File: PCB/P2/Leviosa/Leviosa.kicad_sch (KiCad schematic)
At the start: 52 parts, among them J1 2.54mm 1x03 Servo 1, J2 2.54mm 1x03 Servo 1, J3 2.54mm 1x03 Spare, J4 Barrel_Jack, Q3 TIP122, Q4 TIP122, U1 LM324, U2 ATtiny13A-P, U3 TPS1H200AQDGNRQ1, U4 AMS1117-5.0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

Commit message: update some PCB components as part of P2 iteration
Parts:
- removed D1: BZT52C8V2 WD, Diode_SMD:D_SOD-123, symbol Device:D_Zener
- removed D2, D3: LED, LED_SMD:LED_0805_2012Metric, symbol Device:LED
- removed JP1, JP2, JP3, JP4, JP5, JP6: SolderJumper_2_Open, Jumper:SolderJumper-2_P1.3mm_Open_Pad1.0x1.5mm, symbol Jumper:SolderJumper_2_Open
- removed Pot2: 3362S-1-103LF, Potentiometer_THT:Potentiometer_ACP_CA6-H2,5_Horizontal, symbol Device:R_Potentiometer_US
- removed Q3, Q4: TIP122, Package_TO_SOT_THT:TO-220-3_Vertical, symbol Transistor_BJT:TIP122
- removed R7: 1kΩ, Resistor_SMD:R_0805_2012Metric_Pad1.20x1.40mm_HandSolder, symbol Device:R_US
- removed R8: 400, Resistor_SMD:R_0805_2012Metric_Pad1.20x1.40mm_HandSolder, symbol Device:R_US
- removed U1: LM324, Package_DIP:DIP-14_W7.62mm, symbol Amplifier_Operational:LM324
- added Q1, Q2: NCE0110K, Package_TO_SOT_SMD:TO-252-2, symbol Transistor_FET:DMN61D8LQ
- added U5: LM393, Package_SO:SOIC-8_5.3x5.3mm_P1.27mm, symbol Comparator:LM393
- C4: value 10µF -> 22µF
- R2: value 100kΩ -> 51kΩ; Link https://jlcpcb.com/partdetail/738376-RCT06100KFLF/C702843 -> https://jlcpcb.com/partdetail/23923-0603WAF5102T5E/C23196
- R3: value 7.8kΩ -> 4kΩ
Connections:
- net 5V: now also U5.8 (V+)
- net GND: now also Q2.3 (D), U5.4 (V-)
- net PB2: no longer U6.3 (VOUT)
- net coil_output: now also Q1.2 (S)
- net no_magnet_point: now also U5.5 (+)
- net no_magnet_point_trigger: now also U5.7
- net set_point: now also U5.2 (-)
- net set_point_trigger: now also U5.1
- net transistor1_output: now also Q1.3 (D), Q2.2 (S)
- net at R1.1, TP6.1: now also Q1.1 (G)
- net at R6.1, TP7.1: now also Q2.1 (G)
- new net hall_output: U5.3 (+), U5.6 (-), U6.3 (VOUT)
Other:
- note added: "(12V - 9.6V)/5ma = 460 Ohm minimum"
- note added: "TODO change from voltage divider to a static set point. Check setup to ensure correct voltage set here."
- note added: "TODO: current sense from coil"
- note added: "voltage divider: ~[0.308V, 1.077V] ~[63, 220] analogRead()"
- note removed: "(12V - 9.6V)/5ma = 460 Not sure if this calc is right so keep it to 1K for now"
- note removed: "(5V - 2.2V)/ 5ma = 560"
- note removed: "See (1)"
- note removed: "voltage divider: ~[0.331V, 0.756V] ~[68, 155] analogRead()"
- note removed: "voltage divider: ~[1.65V, 1.96V] ~[337, 399] analogRead()"
- moved on the sheet: C1, C2, C4, D4, D6, R13, R14, R9, TP1, TP2, TP4, U3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

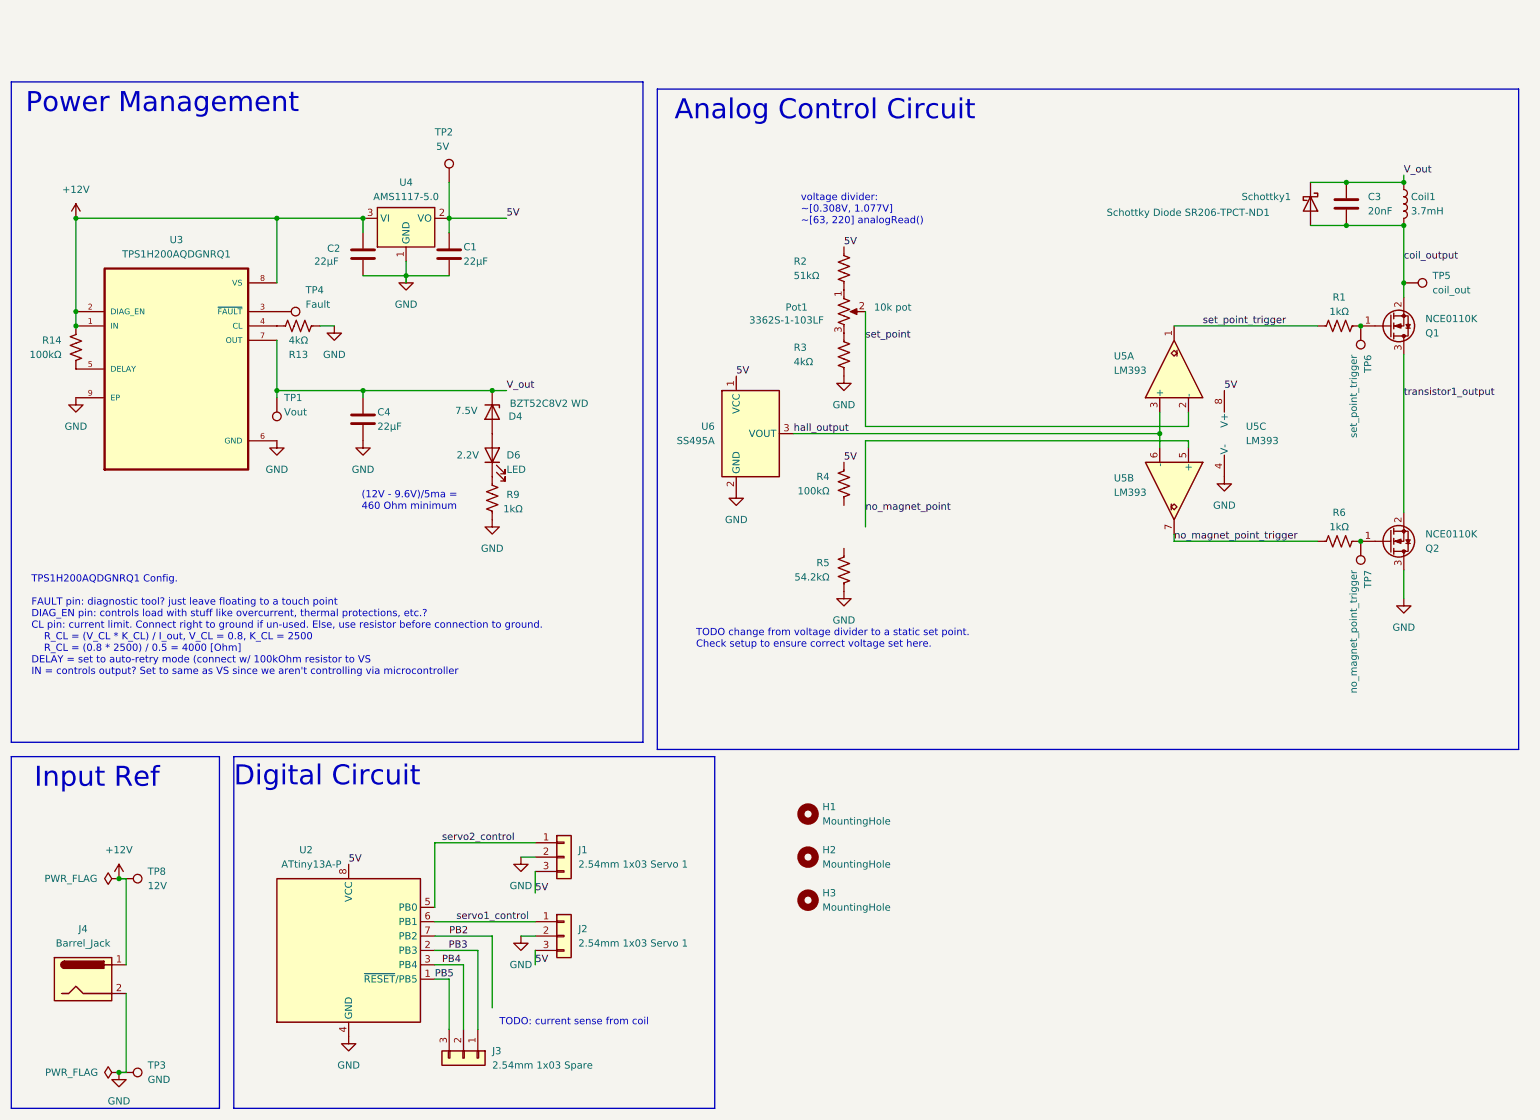
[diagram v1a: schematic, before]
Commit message: swap components, add start of current sense circuit
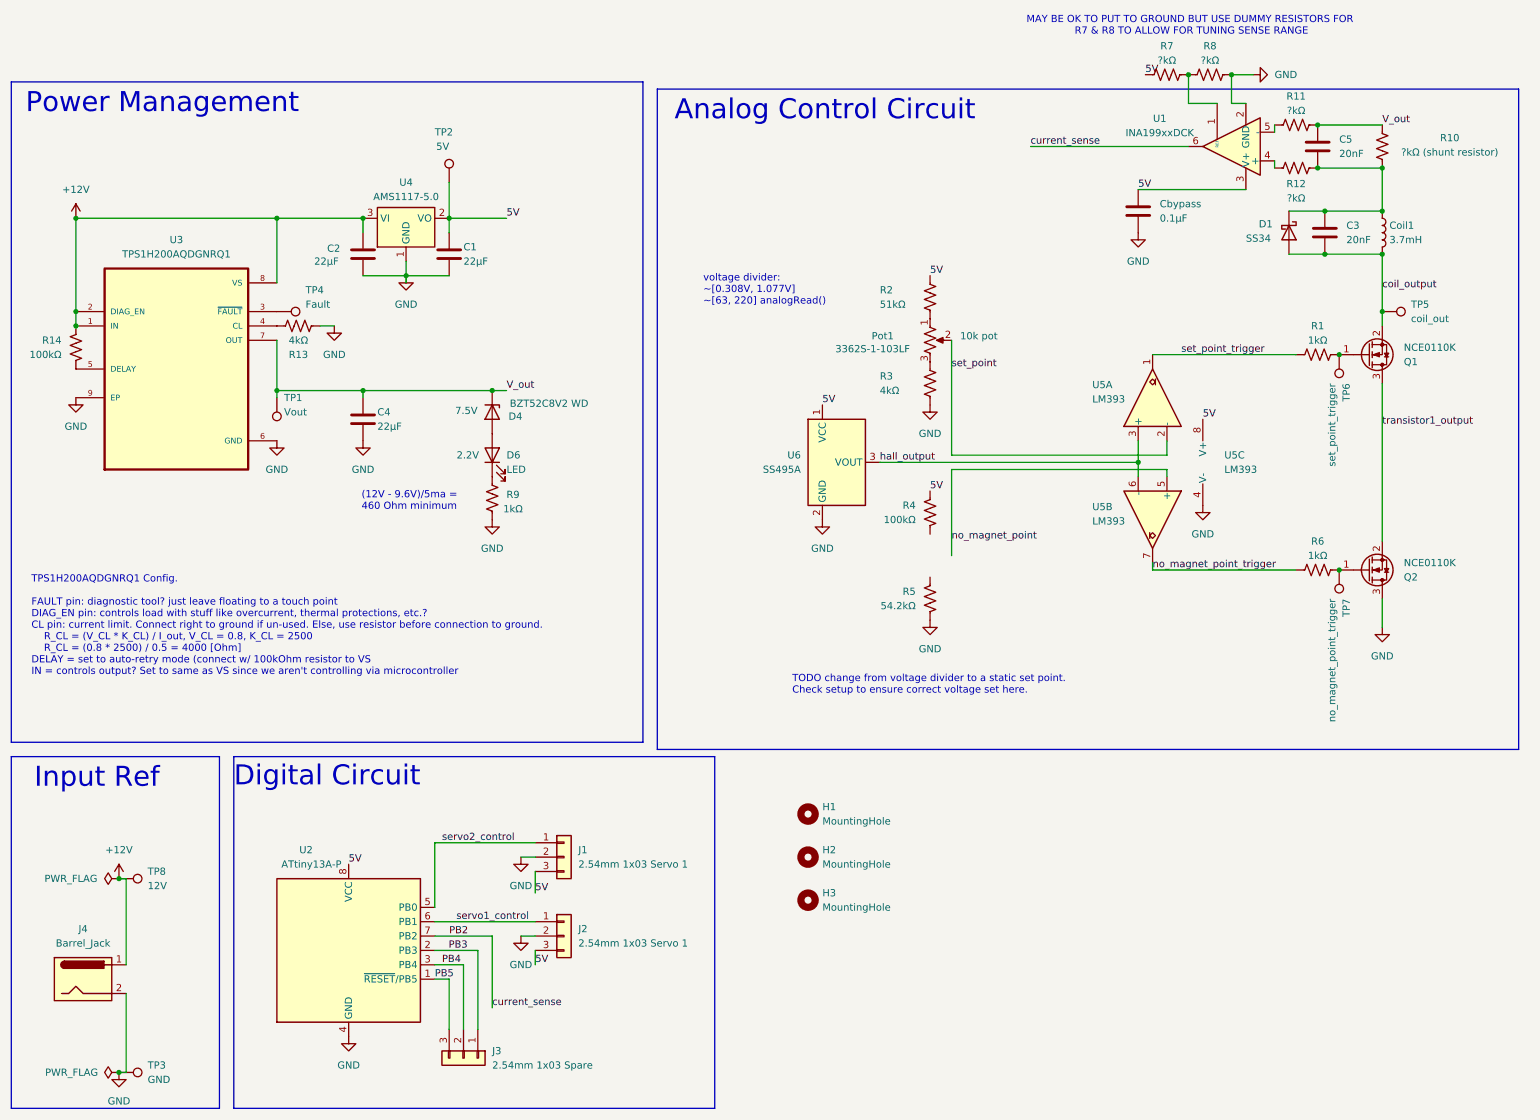
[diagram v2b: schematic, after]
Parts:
- removed Schottky1: Schottky Diode SR206-TPCT-ND1, B230A_13_F:SMA_DIO, symbol Device:D_Schottky
- added C5: 20nF, Capacitor_SMD:C_0805_2012Metric_Pad1.18x1.45mm_HandSolder, symbol Device:C
- added Cbypass: 0.1µF, Capacitor_SMD:C_0805_2012Metric_Pad1.18x1.45mm_HandSolder, symbol Device:C
- added D1: SS34, Diode_SMD:D_SMA, symbol Diode:SS34
- added R10: ?kΩ (shunt resistor), Resistor_SMD:R_0805_2012Metric_Pad1.20x1.40mm_HandSolder, symbol Device:R_US
- added R11, R12, R7, R8: ?kΩ, Resistor_SMD:R_0805_2012Metric_Pad1.20x1.40mm_HandSolder, symbol Device:R_US
- added U1: INA199xxDCK, Package_TO_SOT_SMD:SOT-363_SC-70-6, symbol Amplifier_Current:INA199xxDCK
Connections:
- net 5V: now also Cbypass.1, R7.2, U1.3 (V+)
- net GND: now also Cbypass.2, R8.1, U1.2 (GND)
- net PB2: now also U1.6
- net V_out: now also C5.1, R10.2, R11.1; no longer C3.1, Coil1.1
- net coil_output: now also D1.2 (A)
- new net: C3.1, C5.2, Coil1.1, D1.1 (K), R10.1, R12.1
- new net: R12.2, U1.4 (+)
- new net: R7.1, R8.2, U1.1 (REF)
- new net: R11.2, U1.5 (-)
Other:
- note added: "MAY BE OK TO PUT TO GROUND BUT USE DUMMY RESISTORS FOR R7 & R8 TO ALLOW FOR TUNING SENSE RANGE"
- note removed: "TODO: current sense from coil"
- moved on the sheet: C3, Coil1, Pot1, Q1, Q2, R1, R2, R3, R4, R5, R6, TP5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

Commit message: flesh out schematic
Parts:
- C5: value 20nF -> ?nF
- R7, R8: value ?kΩ -> DNP
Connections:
- net no_magnet_point: now also R4.1, R5.2
- net at R3.2: now also Pot1.1; no longer Pot1.3
- net at R2.1: now also Pot1.3; no longer Pot1.1
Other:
- note added: "R7 and R8: - short R8 to ground for base case - put in voltage divider if needed to offset current readings"
- note added: "RC filter: ?"
- note added: "voltage divider: ~[0.308V, 1.077V] ~[63, 220] analogRead"
- note removed: "MAY BE OK TO PUT TO GROUND BUT USE DUMMY RESISTORS FOR R7 & R8 TO ALLOW FOR TUNING SENSE RANGE"
- note removed: "voltage divider: ~[0.308V, 1.077V] ~[63, 220] analogRead()"
- moved on the sheet: C3, C5, Cbypass, Coil1, D1, H1, H2, H3, Pot1, Q1, Q2, R1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

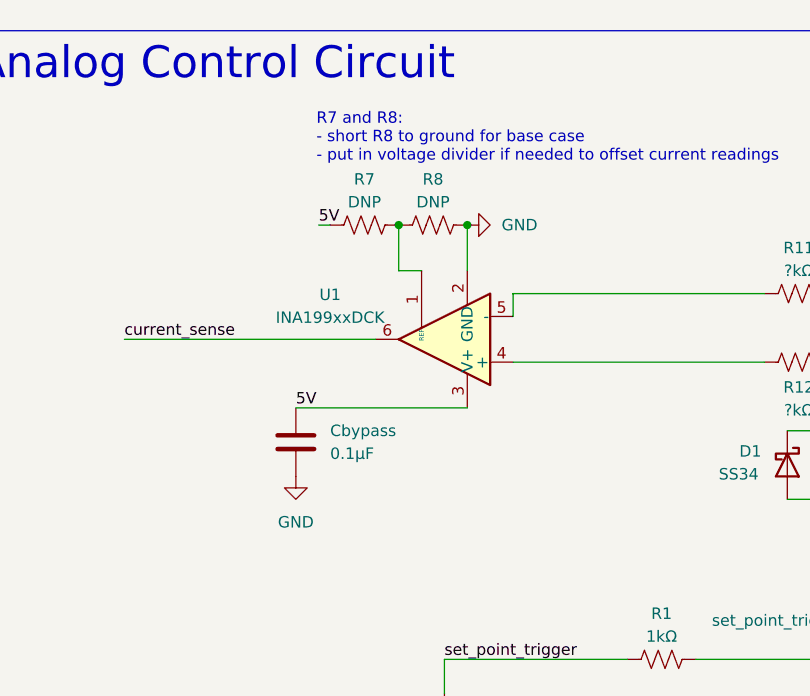
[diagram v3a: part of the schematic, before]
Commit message: fix inputs to current sense
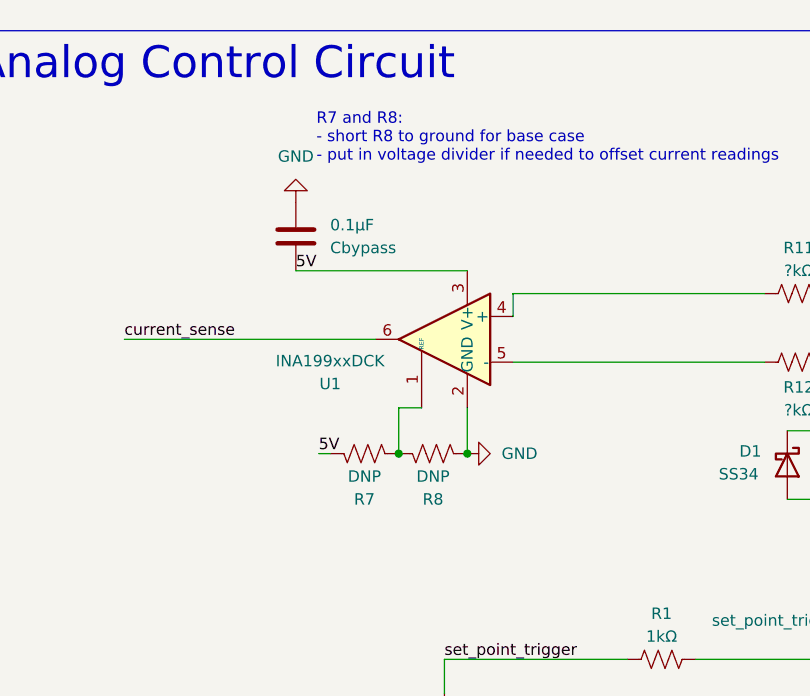
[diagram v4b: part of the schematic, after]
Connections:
- net at R12.2: now also U1.5 (-); no longer U1.4 (+)
- net at R11.2: now also U1.4 (+); no longer U1.5 (-)
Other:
- moved on the sheet: Cbypass, R7, R8, U1
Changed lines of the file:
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@@
 	)
 	(junction
-		(at 204.47 36.83)
+		(at 204.47 62.23)
 		(diameter 0)
 		(color 0 0 0 0)
@@
 	)
 	(junction
-		(at 196.85 36.83)
+		(at 196.85 62.23)
 		(diameter 0)
 		(color 0 0 0 0)
@@
 	(wire
 		(pts
-			(xy 196.85 41.91) (xy 199.39 41.91)
+			(xy 196.85 57.15) (xy 199.39 57.15)
 		)
 		(stroke
@@
 	(wire
 		(pts
-			(xy 196.85 36.83) (xy 196.85 41.91)
+			(xy 196.85 62.23) (xy 196.85 57.15)
 		)
 		(stroke
@@
 	(wire
 		(pts
-			(xy 187.96 36.83) (xy 189.23 36.83)
+			(xy 187.96 62.23) (xy 189.23 62.23)
 		)
 		(stroke
@@
 	(wire
 		(pts
-			(xy 185.42 57.15) (xy 204.47 57.15)
+			(xy 185.42 41.91) (xy 204.47 41.91)
 		)
 		(stroke
@@
 	(wire
 		(pts
-			(xy 204.47 36.83) (xy 204.47 41.91)
+			(xy 204.47 62.23) (xy 204.47 57.15)
 		)
 		(stroke
@@
 	)
 	(label "5V"
-		(at 185.42 57.15 0)
+		(at 185.42 41.91 0)
 		(effects
 			(font
@@
 	)
 	(label "5V"
-		(at 187.96 36.83 0)
+		(at 187.96 62.23 0)
 		(effects
 			(font
@@
 	(symbol
 		(lib_id "Device:C")
-		(at 185.42 60.96 0)
+		(at 185.42 38.1 0)
+		(mirror x)
 		(unit 1)
 		(exclude_from_sim no)
@@
 		(fields_autoplaced yes)
 		(property "Reference" "Cbypass"
-			(at 189.23 59.6899 0)
+			(at 189.23 39.3701 0)
 			(effects
 				(font
@@
 		)
 		(property "Value" "0.1µF"
-			(at 189.23 62.2299 0)
+			(at 189.23 36.8301 0)
 			(effects
 				(font
@@
 		)
 		(property "Footprint" "Capacitor_SMD:C_0805_2012Metric_Pad1.18x1.45mm_HandSolder"
-			(at 186.3852 64.77 0)
+			(at 186.3852 34.29 0)
 			(effects
 				(font
@@
 		)
 		(property "Datasheet" "~"
-			(at 185.42 60.96 0)
+			(at 185.42 38.1 0)
 			(effects
 				(font
@@
 		)
 		(property "Description" ""
-			(at 185.42 60.96 0)
+			(at 185.42 38.1 0)
 			(effects
 				(font
@@
 		)
 		(property "Link" ""
-			(at 185.42 60.96 0)
+			(at 185.42 38.1 0)
 			(effects
 				(font
@@
 	(symbol
 		(lib_id "Amplifier_Current:INA199xxDCK")
-		(at 201.93 49.53 180)
+		(at 201.93 49.53 0)
+		(mirror y)
 		(unit 1)
 		(exclude_from_sim no)
@@
 		(fields_autoplaced yes)
 		(property "Reference" "U1"
-			(at 189.23 44.5768 0)
+			(at 189.23 54.4832 0)
 			(effects
 				(font
@@
 		)
 		(property "Value" "INA199xxDCK"
-			(at 189.23 47.1168 0)
+			(at 189.23 51.9432 0)
 			(effects
 				(font
@@
 		)
 		(property "Footprint" "Package_TO_SOT_SMD:SOT-363_SC-70-6"
-			(at 200.66 50.8 0)
+			(at 200.66 48.26 0)
 			(effects
 				(font
@@
 		)
 		(property "Datasheet" "http://www.ti.com/lit/ds/symlink/ina199.pdf"
-			(at 198.12 53.34 0)
+			(at 198.12 45.72 0)
 			(effects
 				(font
@@
 	(symbol
 		(lib_id "power:GND")
-		(at 185.42 64.77 0)
+		(at 185.42 34.29 0)
+		(mirror x)
 		(unit 1)
 		(exclude_from_sim no)
@@
 		(on_board yes)
 		(dnp no)
-		(fields_autoplaced yes)
 		(property "Reference" "#PWR04"
-			(at 185.42 71.12 0)
+			(at 185.42 27.94 0)
 			(effects
 				(font
@@
 		)
 		(property "Value" "GND"
-			(at 185.42 69.85 0)
+			(at 185.42 29.21 0)
 			(effects
 				(font
@@
 		)
 		(property "Footprint" ""
-			(at 185.42 64.77 0)
+			(at 185.42 34.29 0)
 			(effects
 				(font
@@
 		)
 		(property "Datasheet" ""
-			(at 185.42 64.77 0)
+			(at 185.42 34.29 0)
 			(effects
 				(font
@@
 		)
 		(property "Description" ""
-			(at 185.42 64.77 0)
+			(at 185.42 34.29 0)
 			(effects
 				(font
@@
 	(symbol
 		(lib_id "power:GND")
-		(at 204.47 36.83 90)
+		(at 204.47 62.23 90)
+		(mirror x)
 		(unit 1)
 		(exclude_from_sim no)
@@
 		(fields_autoplaced yes)
 		(property "Reference" "#PWR016"
-			(at 210.82 36.83 0)
+			(at 210.82 62.23 0)
 			(effects
 				(font
@@
 		)
 		(property "Value" "GND"
-			(at 208.28 36.8299 90)
+			(at 208.28 62.2301 90)
 			(effects
 				(font
@@
 		)
 		(property "Footprint" ""
-			(at 204.47 36.83 0)
+			(at 204.47 62.23 0)
 			(effects
 				(font
@@
 		)
 		(property "Datasheet" ""
-			(at 204.47 36.83 0)
+			(at 204.47 62.23 0)
 			(effects
 				(font
@@
 		)
 		(property "Description" ""
-			(at 204.47 36.83 0)
+			(at 204.47 62.23 0)
 			(effects
 				(font
@@
 	(symbol
 		(lib_id "Device:R_US")
-		(at 200.66 36.83 270)
+		(at 200.66 62.23 270)
+		(mirror x)
 		(unit 1)
 		(exclude_from_sim no)
@@
 		(dnp no)
 		(property "Reference" "R8"
-			(at 200.66 31.75 90)
+			(at 200.66 67.31 90)
 			(effects
 				(font
@@
 		)
 		(property "Value" "DNP"
-			(at 200.66 34.29 90)
+			(at 200.66 64.77 90)
 			(effects
 				(font
@@
 		)
 		(property "Footprint" "Resistor_SMD:R_0805_2012Metric_Pad1.20x1.40mm_HandSolder"
-			(at 200.406 37.846 90)
+			(at 200.406 61.214 90)
 			(effects
 				(font
@@
 		)
 		(property "Datasheet" "~"
-			(at 200.66 36.83 0)
+			(at 200.66 62.23 0)
 			(effects
 				(font
@@
 		)
 		(property "Description" ""
-			(at 200.66 36.83 0)
+			(at 200.66 62.23 0)
 			(effects
 				(font
@@
 	(symbol
 		(lib_id "Device:R_US")
-		(at 193.04 36.83 270)
+		(at 193.04 62.23 270)
+		(mirror x)
 		(unit 1)
 		(exclude_from_sim no)
@@
 		(dnp no)
 		(property "Reference" "R7"
-			(at 193.04 31.75 90)
+			(at 193.04 67.31 90)
 			(effects
 				(font
@@
 		)
 		(property "Value" "DNP"
-			(at 193.04 34.29 90)
+			(at 193.04 64.77 90)
 			(effects
 				(font
@@
 		)
 		(property "Footprint" "Resistor_SMD:R_0805_2012Metric_Pad1.20x1.40mm_HandSolder"
-			(at 192.786 37.846 90)
+			(at 192.786 61.214 90)
 			(effects
 				(font
@@
 		)
 		(property "Datasheet" "~"
-			(at 193.04 36.83 0)
+			(at 193.04 62.23 0)
 			(effects
 				(font
@@
 		)
 		(property "Description" ""
-			(at 193.04 36.83 0)
+			(at 193.04 62.23 0)
 			(effects
 				(font
